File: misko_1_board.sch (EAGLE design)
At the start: 151 parts, among them IC1 ATMEGA1281-16AU, IC10 ORG1510-MK4, IC11 TPS3808G33DBVT, IC12 LTC4425, IC13 RN4678_BT_MODULE, IC14 ADXL345, IC15 74HCT1G32, IC16 FM25W256-SOIC, IC17 MICROSD_SPI_MODE, IC18 FH12-30S-0.5SH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

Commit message: - corrected values for oscillator load capacitors
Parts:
- C12, C8: value 15pF -> 7pF
- Q1: value ABM3B -> ABM3B-8MHZ-10-1-U-T
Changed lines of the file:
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@@
 <grid distance="0.1" unitdist="inch" unit="inch" style="lines" multiple="1" display="no" altdistance="0.01" altunitdist="inch" altunit="inch"/>
 <layers>
-<layer number="1" name="Top" color="4" fill="1" visible="yes" active="no"/>
-<layer number="2" name="Route2" color="1" fill="3" visible="yes" active="no"/>
-<layer number="3" name="Route3" color="4" fill="3" visible="yes" active="no"/>
-<layer number="4" name="Route4" color="1" fill="4" visible="yes" active="no"/>
-<layer number="5" name="Route5" color="4" fill="4" visible="yes" active="no"/>
-<layer number="6" name="Route6" color="1" fill="8" visible="yes" active="no"/>
-<layer number="7" name="Route7" color="4" fill="8" visible="yes" active="no"/>
-<layer number="8" name="Route8" color="1" fill="2" visible="yes" active="no"/>
-<layer number="9" name="Route9" color="4" fill="2" visible="yes" active="no"/>
-<layer number="10" name="Route10" color="1" fill="7" visible="yes" active="no"/>
-<layer number="11" name="Route11" color="4" fill="7" visible="yes" active="no"/>
-<layer number="12" name="Route12" color="1" fill="5" visible="yes" active="no"/>
-<layer number="13" name="Route13" color="4" fill="5" visible="yes" active="no"/>
-<layer number="14" name="Route14" color="1" fill="6" visible="yes" active="no"/>
-<layer number="15" name="Route15" color="4" fill="6" visible="yes" active="no"/>
-<layer number="16" name="Bottom" color="1" fill="1" visible="yes" active="no"/>
-<layer number="17" name="Pads" color="2" fill="1" visible="yes" active="no"/>
-<layer number="18" name="Vias" color="2" fill="1" visible="yes" active="no"/>
-<layer number="19" name="Unrouted" color="6" fill="1" visible="yes" active="no"/>
-<layer number="20" name="Dimension" color="15" fill="1" visible="yes" active="no"/>
-<layer number="21" name="tPlace" color="7" fill="1" visible="yes" active="no"/>
-<layer number="22" name="bPlace" color="7" fill="1" visible="yes" active="no"/>
-<layer number="23" name="tOrigins" color="15" fill="1" visible="yes" active="no"/>
-<layer number="24" name="bOrigins" color="15" fill="1" visible="yes" active="no"/>
-<layer number="25" name="tNames" color="7" fill="1" visible="yes" active="no"/>
-<layer number="26" name="bNames" color="7" fill="1" visible="yes" active="no"/>
-<layer number="27" name="tValues" color="7" fill="1" visible="yes" active="no"/>
-<layer number="28" name="bValues" color="7" fill="1" visible="yes" active="no"/>
+<layer number="1" name="Top" color="4" fill="1" visible="no" active="no"/>
+<layer number="2" name="Route2" color="1" fill="3" visible="no" active="no"/>
+<layer number="3" name="Route3" color="4" fill="3" visible="no" active="no"/>
+<layer number="4" name="Route4" color="1" fill="4" visible="no" active="no"/>
+<layer number="5" name="Route5" color="4" fill="4" visible="no" active="no"/>
+<layer number="6" name="Route6" color="1" fill="8" visible="no" active="no"/>
+<layer number="7" name="Route7" color="4" fill="8" visible="no" active="no"/>
+<layer number="8" name="Route8" color="1" fill="2" visible="no" active="no"/>
+<layer number="9" name="Route9" color="4" fill="2" visible="no" active="no"/>
+<layer number="10" name="Route10" color="1" fill="7" visible="no" active="no"/>
+<layer number="11" name="Route11" color="4" fill="7" visible="no" active="no"/>
+<layer number="12" name="Route12" color="1" fill="5" visible="no" active="no"/>
+<layer number="13" name="Route13" color="4" fill="5" visible="no" active="no"/>
+<layer number="14" name="Route14" color="1" fill="6" visible="no" active="no"/>
+<layer number="15" name="Route15" color="4" fill="6" visible="no" active="no"/>
+<layer number="16" name="Bottom" color="1" fill="1" visible="no" active="no"/>
+<layer number="17" name="Pads" color="2" fill="1" visible="no" active="no"/>
+<layer number="18" name="Vias" color="2" fill="1" visible="no" active="no"/>
+<layer number="19" name="Unrouted" color="6" fill="1" visible="no" active="no"/>
+<layer number="20" name="Dimension" color="15" fill="1" visible="no" active="no"/>
+<layer number="21" name="tPlace" color="7" fill="1" visible="no" active="no"/>
+<layer number="22" name="bPlace" color="7" fill="1" visible="no" active="no"/>
+<layer number="23" name="tOrigins" color="15" fill="1" visible="no" active="no"/>
+<layer number="24" name="bOrigins" color="15" fill="1" visible="no" active="no"/>
+<layer number="25" name="tNames" color="7" fill="1" visible="no" active="no"/>
+<layer number="26" name="bNames" color="7" fill="1" visible="no" active="no"/>
+<layer number="27" name="tValues" color="7" fill="1" visible="no" active="no"/>
+<layer number="28" name="bValues" color="7" fill="1" visible="no" active="no"/>
 <layer number="29" name="tStop" color="7" fill="3" visible="no" active="no"/>
 <layer number="30" name="bStop" color="7" fill="6" visible="no" active="no"/>
@@
 <layer number="35" name="tGlue" color="7" fill="4" visible="no" active="no"/>
 <layer number="36" name="bGlue" color="7" fill="5" visible="no" active="no"/>
-<layer number="37" name="tTest" color="7" fill="1" visible="yes" active="no"/>
-<layer number="38" name="bTest" color="7" fill="1" visible="yes" active="no"/>
+<layer number="37" name="tTest" color="7" fill="1" visible="no" active="no"/>
+<layer number="38" name="bTest" color="7" fill="1" visible="no" active="no"/>
 <layer number="39" name="tKeepout" color="4" fill="11" visible="no" active="no"/>
 <layer number="40" name="bKeepout" color="1" fill="11" visible="no" active="no"/>
@@
 <layer number="44" name="Drills" color="7" fill="1" visible="no" active="no"/>
 <layer number="45" name="Holes" color="7" fill="1" visible="no" active="no"/>
-<layer number="46" name="Milling" color="3" fill="1" visible="yes" active="no"/>
-<layer number="47" name="Measures" color="7" fill="1" visible="yes" active="no"/>
-<layer number="48" name="Document" color="7" fill="1" visible="yes" active="no"/>
-<layer number="49" name="Reference" color="7" fill="1" visible="yes" active="no"/>
-<layer number="50" name="dxf" color="7" fill="1" visible="yes" active="no"/>
-<layer number="51" name="tDocu" color="7" fill="1" visible="yes" active="no"/>
-<layer number="52" name="bDocu" color="7" fill="1" visible="yes" active="no"/>
-<layer number="53" name="tGND_GNDA" color="7" fill="9" visible="yes" active="no"/>
-<layer number="54" name="bGND_GNDA" color="1" fill="9" visible="yes" active="no"/>
-<layer number="56" name="wert" color="7" fill="1" visible="yes" active="no"/>
-<layer number="57" name="tCAD" color="7" fill="1" visible="yes" active="no"/>
-<layer number="59" name="tCarbon" color="7" fill="1" visible="yes" active="no"/>
-<layer number="60" name="bCarbon" color="7" fill="1" visible="yes" active="no"/>
+<layer number="46" name="Milling" color="3" fill="1" visible="no" active="no"/>
+<layer number="47" name="Measures" color="7" fill="1" visible="no" active="no"/>
+<layer number="48" name="Document" color="7" fill="1" visible="no" active="no"/>
+<layer number="49" name="Reference" color="7" fill="1" visible="no" active="no"/>
+<layer number="50" name="dxf" color="7" fill="1" visible="no" active="no"/>
+<layer number="51" name="tDocu" color="7" fill="1" visible="no" active="no"/>
+<layer number="52" name="bDocu" color="7" fill="1" visible="no" active="no"/>
+<layer number="53" name="tGND_GNDA" color="7" fill="9" visible="no" active="no"/>
+<layer number="54" name="bGND_GNDA" color="1" fill="9" visible="no" active="no"/>
+<layer number="56" name="wert" color="7" fill="1" visible="no" active="no"/>
+<layer number="57" name="tCAD" color="7" fill="1" visible="no" active="no"/>
+<layer number="59" name="tCarbon" color="7" fill="1" visible="no" active="no"/>
+<layer number="60" name="bCarbon" color="7" fill="1" visible="no" active="no"/>
 <layer number="90" name="Modules" color="5" fill="1" visible="yes" active="yes"/>
 <layer number="91" name="Nets" color="2" fill="1" visible="yes" active="yes"/>
@@
 <part name="R3" library="rcl" deviceset="R-EU_" device="R0805" value="4k7"/>
 <part name="C3" library="resistor" library_urn="urn:adsk.eagle:library:348" deviceset="C-EU" device="C0805" value="0.1µF"/>
-<part name="C8" library="resistor" library_urn="urn:adsk.eagle:library:348" deviceset="C-EU" device="C0805" value="15pF"/>
-<part name="C12" library="resistor" library_urn="urn:adsk.eagle:library:348" deviceset="C-EU" device="C0805" value="15pF"/>
+<part name="C8" library="resistor" library_urn="urn:adsk.eagle:library:348" deviceset="C-EU" device="C0805" value="7pF"/>
+<part name="C12" library="resistor" library_urn="urn:adsk.eagle:library:348" deviceset="C-EU" device="C0805" value="7pF"/>
 <part name="D1" library="Diode2" deviceset="1N4148" device=""/>
 <part name="SJ3" library="jumper" deviceset="SJ" device="W" value="RESET"/>
@@
 <part name="IC10" library="ORG1510-MK4 GPS module" deviceset="ORG1510-MK4" device=""/>
 <part name="SW1" library="Wurth_Elektronik_Electromechanic_Switch_rev17c" library_urn="urn:adsk.eagle:library:480" deviceset="430152050836" device="" value="RESET"/>
-<part name="Q1" library="ABM3B-8MHZ-10-1-U-T - Quartz Resonator" deviceset="ABM3B" device=""/>
+<part name="Q1" library="ABM3B-8MHZ-10-1-U-T - Quartz Resonator" deviceset="ABM3B" device="" value="ABM3B-8MHZ-10-1-U-T"/>
 <part name="CONN4" library="MX-67503-1230 USB Mini-B SMT straight socket" deviceset="MX-67503-1230" device="" value="USB mini B"/>
 <part name="TP2" library="testpad" deviceset="TP" device="PAD1-17Y" value="GND"/>

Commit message: - named FTDI RX/TX LEDs properly in schematic and on board layout (tplace)
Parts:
- LED1: value yellow -> TX
- LED2: value yellow -> RX
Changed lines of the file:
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@@
 <part name="R4" library="rcl" deviceset="R-EU_" device="R0805" value="3k3"/>
 <part name="R5" library="rcl" deviceset="R-EU_" device="R0805" value="3k3"/>
-<part name="LED2" library="led" library_urn="urn:adsk.eagle:library:259" deviceset="LED" device="CHIPLED_1206" value="yellow"/>
-<part name="LED1" library="led" library_urn="urn:adsk.eagle:library:259" deviceset="LED" device="CHIPLED_1206" value="yellow"/>
+<part name="LED2" library="led" library_urn="urn:adsk.eagle:library:259" deviceset="LED" device="CHIPLED_1206" value="RX"/>
+<part name="LED1" library="led" library_urn="urn:adsk.eagle:library:259" deviceset="LED" device="CHIPLED_1206" value="TX"/>
 <part name="R14" library="resistor" library_urn="urn:adsk.eagle:library:348" deviceset="R-EU_" device="R0805" value="1k"/>
 <part name="R15" library="resistor" library_urn="urn:adsk.eagle:library:348" deviceset="R-EU_" device="R0805" value="1k"/>

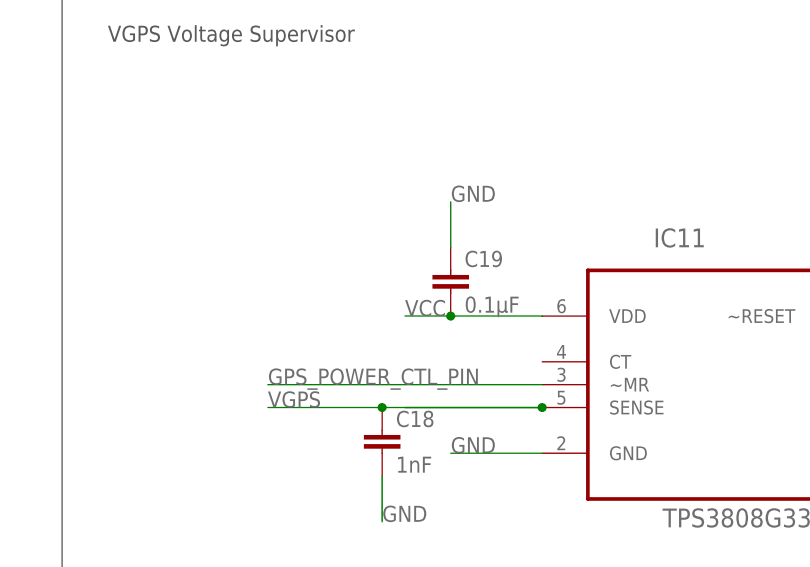
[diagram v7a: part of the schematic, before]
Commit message: - added pulldown (R23) to GPS_POWER_CTL_PIN so that the receiver is turned off when micro controller resets
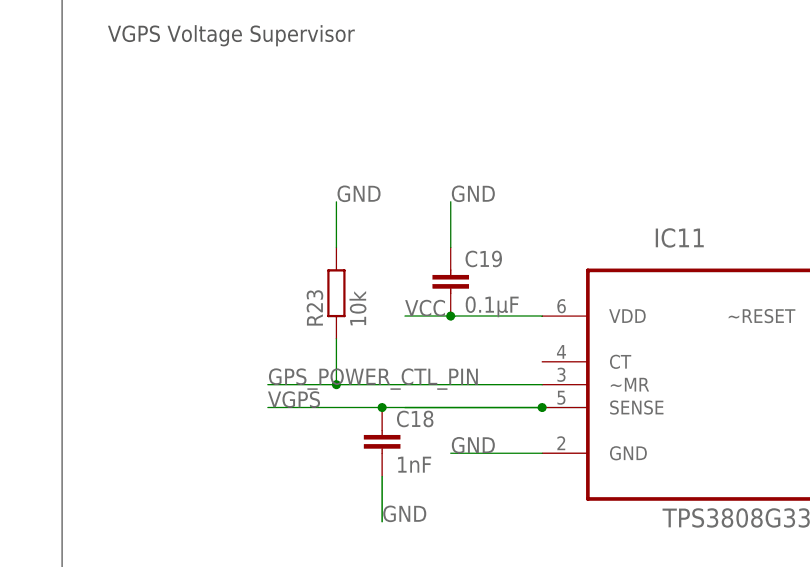
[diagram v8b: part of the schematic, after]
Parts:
- added R23: 10k, resistor:R-EU_R0805
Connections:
- net GND: now also R23.2
- net GPS_POWER_CTL_PIN: now also R23.1
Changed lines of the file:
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@@
 <part name="D6" library="zener" library_urn="urn:adsk.eagle:library:449000" deviceset="ZENER" device="SOD123" package3d_urn="urn:adsk.eagle:package:449003/1" value="1N4733AW-TP"/>
 <part name="D7" library="zener" library_urn="urn:adsk.eagle:library:449000" deviceset="ZENER" device="" value="BZG05C3V6-E3-TR3"/>
+<part name="R23" library="resistor" library_urn="urn:adsk.eagle:library:348" deviceset="R-EU_" device="R0805" value="10k"/>
 </parts>
 <sheets>
@@
 <attribute name="VALUE" x="107.823" y="520.7" size="1.778" layer="96" rot="R90"/>
 </instance>
+<instance part="R23" gate="G$1" x="149.86" y="66.04" rot="R90"/>
 </instances>
 <busses>
@@
 <label x="111.76" y="535.94" size="1.778" layer="95"/>
 </segment>
+<segment>
+<pinref part="R23" gate="G$1" pin="2"/>
+<wire x1="149.86" y1="71.12" x2="149.86" y2="76.2" width="0.1524" layer="91"/>
+<label x="149.86" y="76.2" size="1.778" layer="95"/>
+</segment>
 </net>
 <net name="5V0" class="1">
@@
 <segment>
 <pinref part="IC11" gate="A" pin="~MR"/>
-<wire x1="172.72" y1="55.88" x2="142.24" y2="55.88" width="0.1524" layer="91"/>
+<wire x1="172.72" y1="55.88" x2="149.86" y2="55.88" width="0.1524" layer="91"/>
 <label x="142.24" y="55.88" size="1.778" layer="95"/>
-</segment>
-<segment>
+<pinref part="R23" gate="G$1" pin="1"/>
+<wire x1="149.86" y1="55.88" x2="142.24" y2="55.88" width="0.1524" layer="91"/>
+<wire x1="149.86" y1="60.96" x2="149.86" y2="55.88" width="0.1524" layer="91"/>
+<junction x="149.86" y="55.88"/>
+</segment>
+<segment>
